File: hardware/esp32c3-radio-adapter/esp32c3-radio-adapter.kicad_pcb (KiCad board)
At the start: 2 copper layers, 29 x 38 mm, 13 parts, among them J1 Conn_01x08, J2 Conn_01x08, J3 E07-M1101D_or_Ra-02, J4 Expansion, J5 DIO2/DATA

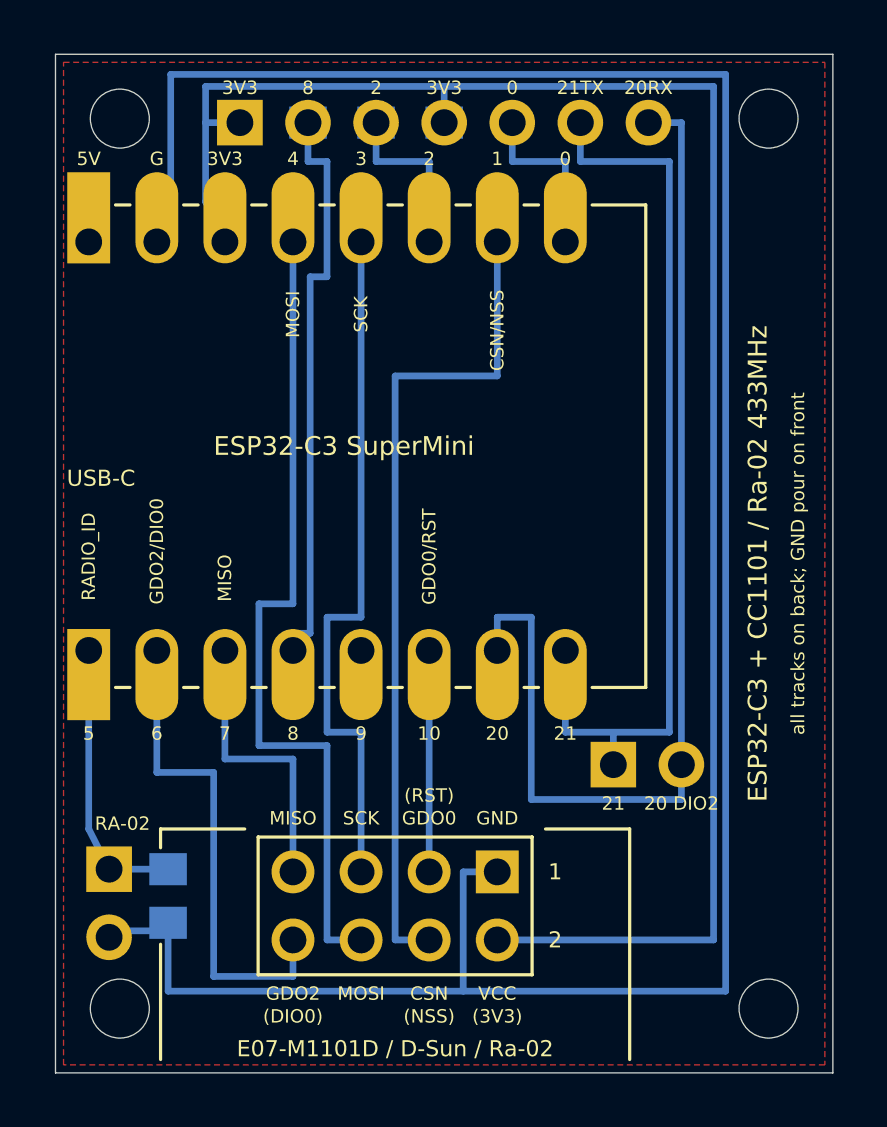
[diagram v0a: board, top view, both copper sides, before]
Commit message: Socket adapter: R4, a GPIO9 pull-up footprint, and clearer silkscreen
GPIO9 is the boot strap the socket no longer carries.  Give it the same
optional do-not-populate 4k7 pull-up to 3V3 the other two straps have.
Its pad is boxed in on the back copper (SCK passes left of it and drops
into the socket pin directly beneath, CSN passes right of it), so:
SCK steps one gap left as soon as it leaves its pad, J4 pins 3 and 4
swap so the second 3V3 sits left of GPIO2 like the first sits left of
GPIO8, and that 3V3 pin feeds down through the power row's GPIO3/GPIO2
gap into R4, whose other pad drops into GPIO9.  CSN keeps right of R4
until it is above the GPIO row's rings.  Still every track on B.Cu; DRC
clean.

Silkscreen: every SuperMini pin now has an inner label (NC, GND, 3V3,
J4, J4/J5, R4, JP1, DIO2 for the pins that carried none); the USB-C is
drawn as its outline instead of a word, solid on the front and dashed
on the back; every outline on the back is dashed; the "all tracks"
notes go, replaced by "parts this side" on the front.  Under the USB-C
outline the two columns' labels are shortened or split into two lines.

Co-Authored-By: Claude Opus 5 (1M context) <noreply@anthropic.com>
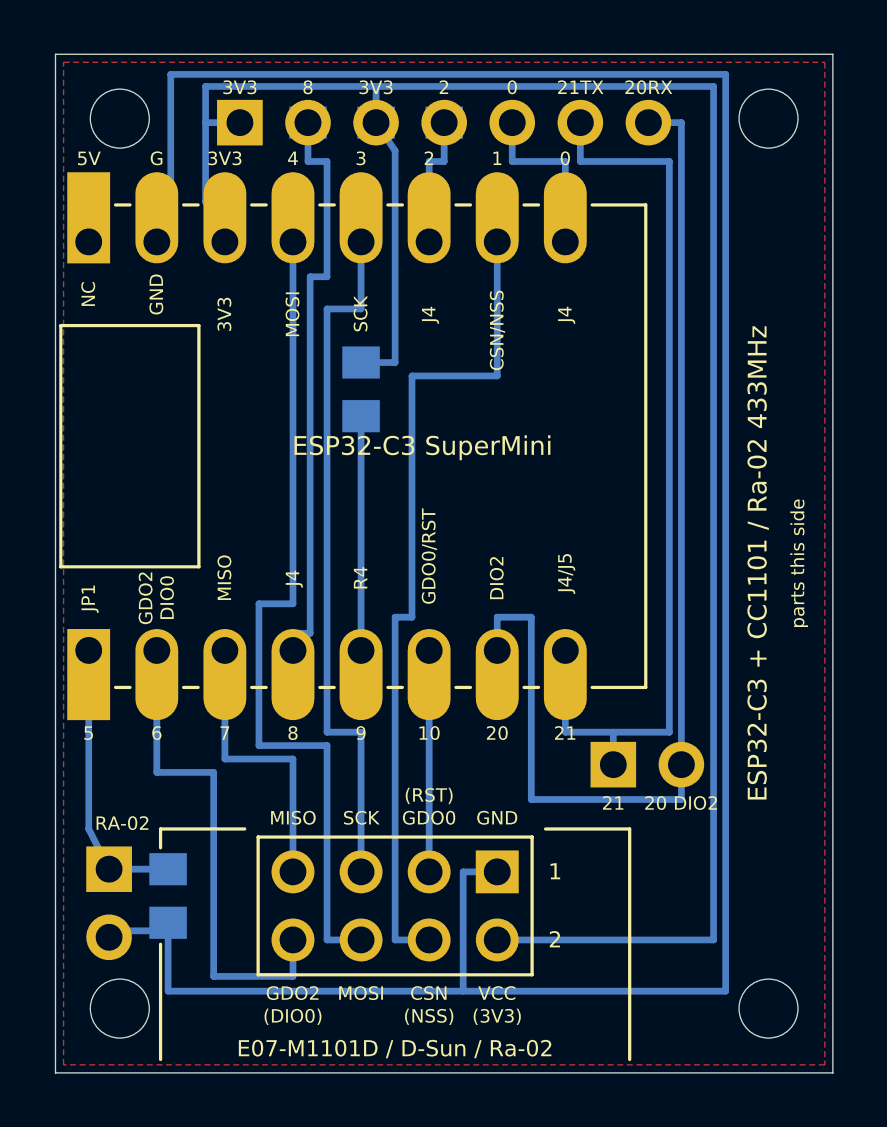
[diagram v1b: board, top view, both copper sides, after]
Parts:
- added R4: 4k7, Adapter:R_0805_2012Metric_HandSolder_AlongY_Back, F.Cu at (111.4, 112.5)
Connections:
- J4 pad 3: GPIO2 -> +3V3
- J4 pad 4: +3V3 -> GPIO2
- R3 pad 1: GPIO2 -> +3V3
- R3 pad 2: +3V3 -> GPIO2
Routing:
- net +3V3: track 67.5 -> 77.9 mm
- net GPIO9: track 0.00 -> 8.74 mm
- net GPIO2: track 6.43 -> 5.01 mm
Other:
- board text added: "DIO0"
- board text added: "DIO2"
- board text added: "J4"
- board text added: "J4/J5"
- board text added: "JP1"
- board text added: "NC"
- board text added: "R4"
- board text added: "parts this side"
- board text removed: "GDO2/DIO0"
- board text removed: "RADIO_ID"
- board text removed: "USB-C"
- board text removed: "all tracks on back; GND pour on front"
- board text removed: "all tracks this side"
